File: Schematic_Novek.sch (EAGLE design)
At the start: 46 parts, among them IC1 STM32F10XCXT6, J2 1X2-3.5MM, J3 1X2-3.5MM, Q1 2N2907, U1 BQ21040, U2 MAX17048G+T10, U3 HX711

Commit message: Component placement on board
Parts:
- removed JP3: (no value), pinhead:PINHD-1X4
- removed R1: (no value), resistor:R-EU_0204/7
- added R13: 1M, SparkFun-Resistors:1MOHM-0603-1/4W-5%
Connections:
- removed net 5V: JP3.3
- removed net FTDI_RX: IC1PORTA_H.PA9, JP3.1
- removed net FTDI_TX: IC1PORTA_H.PA10, JP3.2
- net GND: now also J1.SHIELD, J2.1; no longer JP3.4
- net OSCIN: now also R13.2; no longer R1.2
- net OSCOUT: now also R13.1; no longer R1.1
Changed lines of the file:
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@@
 <part name="C1" library="SparkFun-Capacitors" deviceset="22PF" device="-0603-50V-5%" value="22pF"/>
 <part name="C2" library="SparkFun-Capacitors" deviceset="22PF" device="-0603-50V-5%" value="22pF"/>
-<part name="R1" library="resistor" deviceset="R-EU_" device="0204/7"/>
 <part name="JP1" library="pinhead" library_urn="urn:adsk.eagle:library:325" deviceset="PINHD-1X4" device="/90" package3d_urn="urn:adsk.eagle:package:22404/2" value="SWD"/>
 <part name="FRAME2" library="frames" deviceset="A4L-LOC" device=""/>
@@
 <part name="R3" library="SparkFun-Resistors" deviceset="100KOHM" device="-0603-1/10W-1%" value="100k"/>
 <part name="R4" library="SparkFun-Resistors" deviceset="100KOHM" device="-0603-1/10W-1%" value="100k"/>
-<part name="JP3" library="pinhead" library_urn="urn:adsk.eagle:library:325" deviceset="PINHD-1X4" device="" package3d_urn="urn:adsk.eagle:package:22407/2"/>
 <part name="J1" library="SparkFun-Connectors" deviceset="USB_MICRO-B" device="_FEMALE-SMT"/>
 <part name="SUPPLY15" library="supply2" deviceset="GND" device=""/>
@@
 <part name="J4" library="SparkFun-Connectors" deviceset="CONN_03" device="JST-PTH"/>
 <part name="R12" library="SparkFun-Resistors" deviceset="10KOHM" device="-0603-1/10W-1%" value="10k"/>
+<part name="R13" library="SparkFun-Resistors" deviceset="1MOHM" device="-0603-1/4W-5%" value="1M"/>
 </parts>
 <sheets>
@@
 <attribute name="VALUE" x="185.841" y="74.476" size="1.778" layer="96" font="vector" rot="R270"/>
 </instance>
-<instance part="R1" gate="G$1" x="173" y="81" smashed="yes" rot="R90">
-<attribute name="NAME" x="171.5014" y="77.19" size="1.778" layer="95" rot="R90"/>
-<attribute name="VALUE" x="176.302" y="77.19" size="1.778" layer="96" rot="R90"/>
-</instance>
 <instance part="JP1" gate="A" x="30.96" y="98.46" smashed="yes" rot="MR0">
 <attribute name="NAME" x="37.31" y="106.715" size="1.778" layer="95" rot="MR0"/>
@@
 <attribute name="VALUE" x="194" y="101.476" size="1.778" layer="96" font="vector" align="top-center"/>
 </instance>
-<instance part="JP3" gate="A" x="32" y="47" smashed="yes" rot="MR0">
-<attribute name="NAME" x="38.35" y="55.255" size="1.778" layer="95" rot="MR0"/>
-<attribute name="VALUE" x="38.35" y="39.38" size="1.778" layer="96" rot="MR0"/>
+<instance part="R13" gate="G$1" x="173" y="81" smashed="yes" rot="R90">
+<attribute name="NAME" x="171.476" y="81" size="1.778" layer="95" font="vector" rot="R90" align="bottom-center"/>
+<attribute name="VALUE" x="174.524" y="81" size="1.778" layer="96" font="vector" rot="R90" align="top-center"/>
 </instance>
 </instances>
@@
 <wire x1="180" y1="83.54" x2="180" y2="87" width="0.1524" layer="91"/>
 <wire x1="180" y1="87" x2="185.46" y2="87" width="0.1524" layer="91"/>
-<pinref part="R1" gate="G$1" pin="2"/>
-<wire x1="173" y1="87" x2="180" y2="87" width="0.1524" layer="91"/>
 <junction x="180" y="87"/>
-<wire x1="173" y1="86.08" x2="173" y2="87" width="0.1524" layer="91"/>
 <wire x1="173" y1="87" x2="160" y2="87" width="0.1524" layer="91"/>
 <label x="160" y="87" size="1.778" layer="95"/>
+<pinref part="R13" gate="G$1" pin="2"/>
+<wire x1="173" y1="86.08" x2="173" y2="87" width="0.1524" layer="91"/>
+<wire x1="173" y1="87" x2="180" y2="87" width="0.1524" layer="91"/>
 </segment>
 </net>
@@
 <wire x1="180" y1="78.46" x2="180" y2="76" width="0.1524" layer="91"/>
 <wire x1="180" y1="76" x2="185.46" y2="76" width="0.1524" layer="91"/>
-<pinref part="R1" gate="G$1" pin="1"/>
-<wire x1="173" y1="76" x2="180" y2="76" width="0.1524" layer="91"/>
 <junction x="180" y="76"/>
-<wire x1="173" y1="75.92" x2="173" y2="76" width="0.1524" layer="91"/>
 <wire x1="173" y1="76" x2="160" y2="76" width="0.1524" layer="91"/>
 <label x="160" y="76" size="1.778" layer="95"/>
+<pinref part="R13" gate="G$1" pin="1"/>
+<wire x1="173" y1="75.92" x2="173" y2="76" width="0.1524" layer="91"/>
+<wire x1="173" y1="76" x2="180" y2="76" width="0.1524" layer="91"/>
 </segment>
 </net>
@@
 <pinref part="JP2" gate="A" pin="6"/>
 <wire x1="190" y1="100.52" x2="183.26" y2="100.52" width="0.1524" layer="91"/>
-</segment>
-<segment>
-<pinref part="JP3" gate="A" pin="4"/>
-<wire x1="34.54" y1="44.46" x2="45" y2="44.46" width="0.1524" layer="91"/>
-<label x="45" y="45" size="1.778" layer="95"/>
 </segment>
 </net>
@@
 </segment>
 </net>
-<net name="FTDI_RX" class="0">
-<segment>
-<pinref part="JP3" gate="A" pin="1"/>
-<wire x1="34.54" y1="52.08" x2="45" y2="52.08" width="0.1524" layer="91"/>
-<label x="45" y="52" size="1.778" layer="95"/>
-</segment>
-<segment>
-<pinref part="IC1" gate="PORTA_H" pin="PA9"/>
-<wire x1="101.6" y1="104.14" x2="91" y2="104.14" width="0.1524" layer="91"/>
-<label x="91" y="105" size="1.778" layer="95"/>
-</segment>
-</net>
-<net name="FTDI_TX" class="0">
-<segment>
-<pinref part="JP3" gate="A" pin="2"/>
-<wire x1="34.54" y1="49.54" x2="45" y2="49.54" width="0.1524" layer="91"/>
-<label x="45" y="50" size="1.778" layer="95"/>
-</segment>
-<segment>
-<pinref part="IC1" gate="PORTA_H" pin="PA10"/>
-<wire x1="101.6" y1="101.6" x2="91" y2="101.6" width="0.1524" layer="91"/>
-<label x="91" y="102" size="1.778" layer="95"/>
-</segment>
-</net>
-<net name="5V" class="0">
-<segment>
-<pinref part="JP3" gate="A" pin="3"/>
-<wire x1="34.54" y1="47" x2="45" y2="47" width="0.1524" layer="91"/>
-<label x="45" y="47" size="1.778" layer="95"/>
-</segment>
-</net>
 <net name="SDA" class="0">
 <segment>
@@
 <pinref part="SUPPLY15" gate="GND" pin="GND"/>
 <junction x="49" y="130.54"/>
+<pinref part="J1" gate="G$1" pin="SHIELD"/>
+<wire x1="41.08" y1="130.92" x2="49" y2="130.92" width="0.1524" layer="91"/>
+<wire x1="49" y1="130.92" x2="49" y2="130.54" width="0.1524" layer="91"/>
 </segment>
 <segment>
@@
 <label x="53" y="48" size="1.778" layer="95"/>
 </segment>
-</net>
+<segment>
+<pinref part="J2" gate="G$1" pin="1"/>
+<pinref part="SUPPLY33" gate="GND" pin="GND"/>
+<wire x1="16.08" y1="141.46" x2="16.08" y2="141" width="0.1524" layer="91"/>
+<wire x1="16.08" y1="141" x2="20.46" y2="141" width="0.1524" layer="91"/>
+</segment>
+</net>

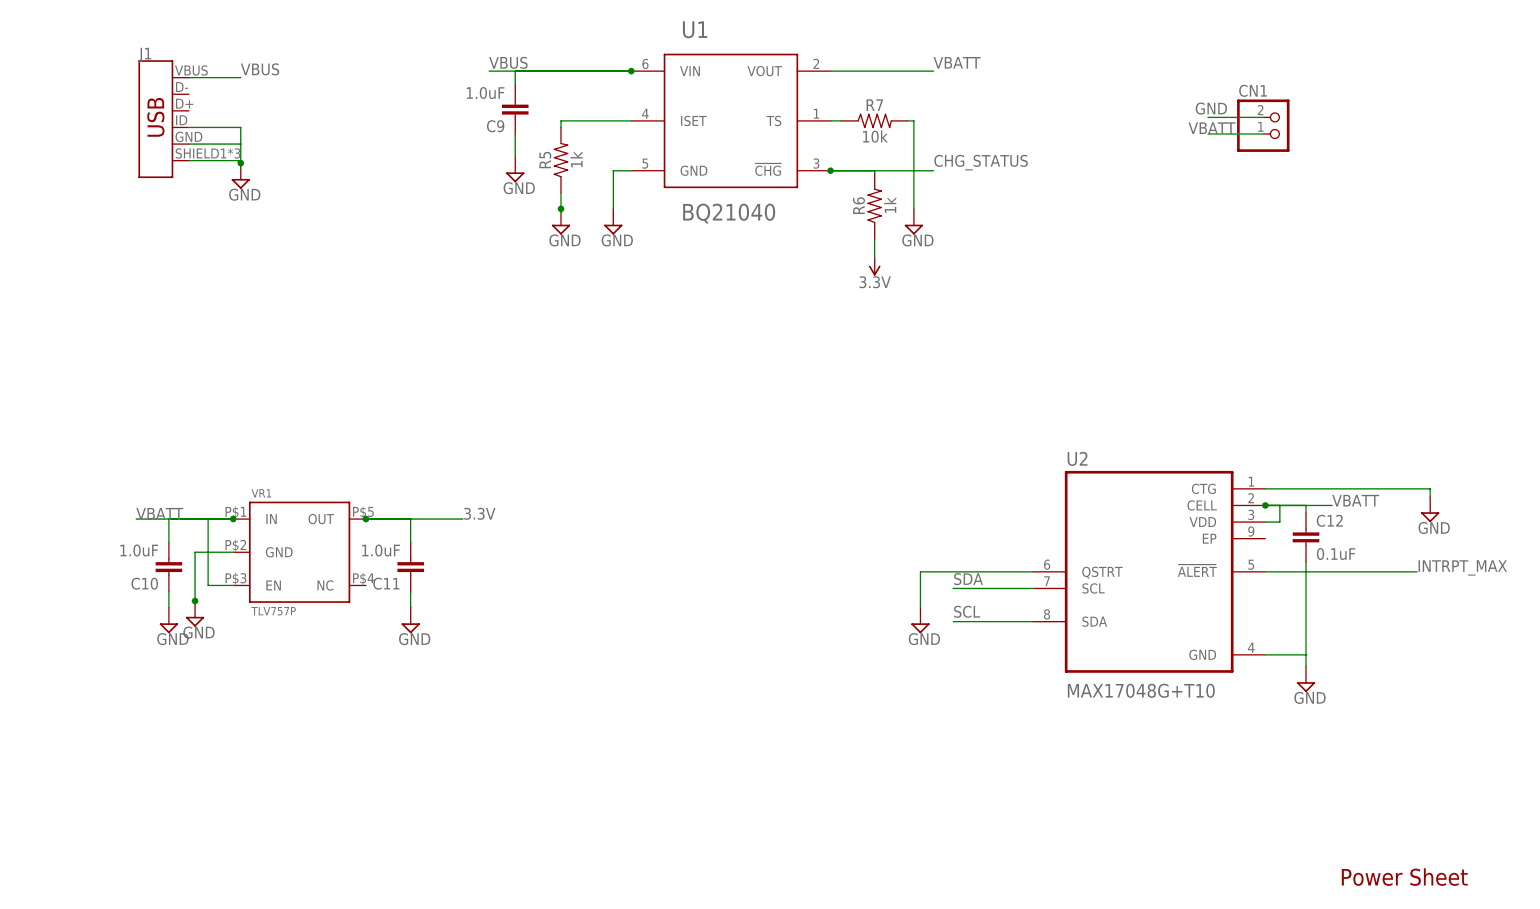
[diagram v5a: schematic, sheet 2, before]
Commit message: Completes routing
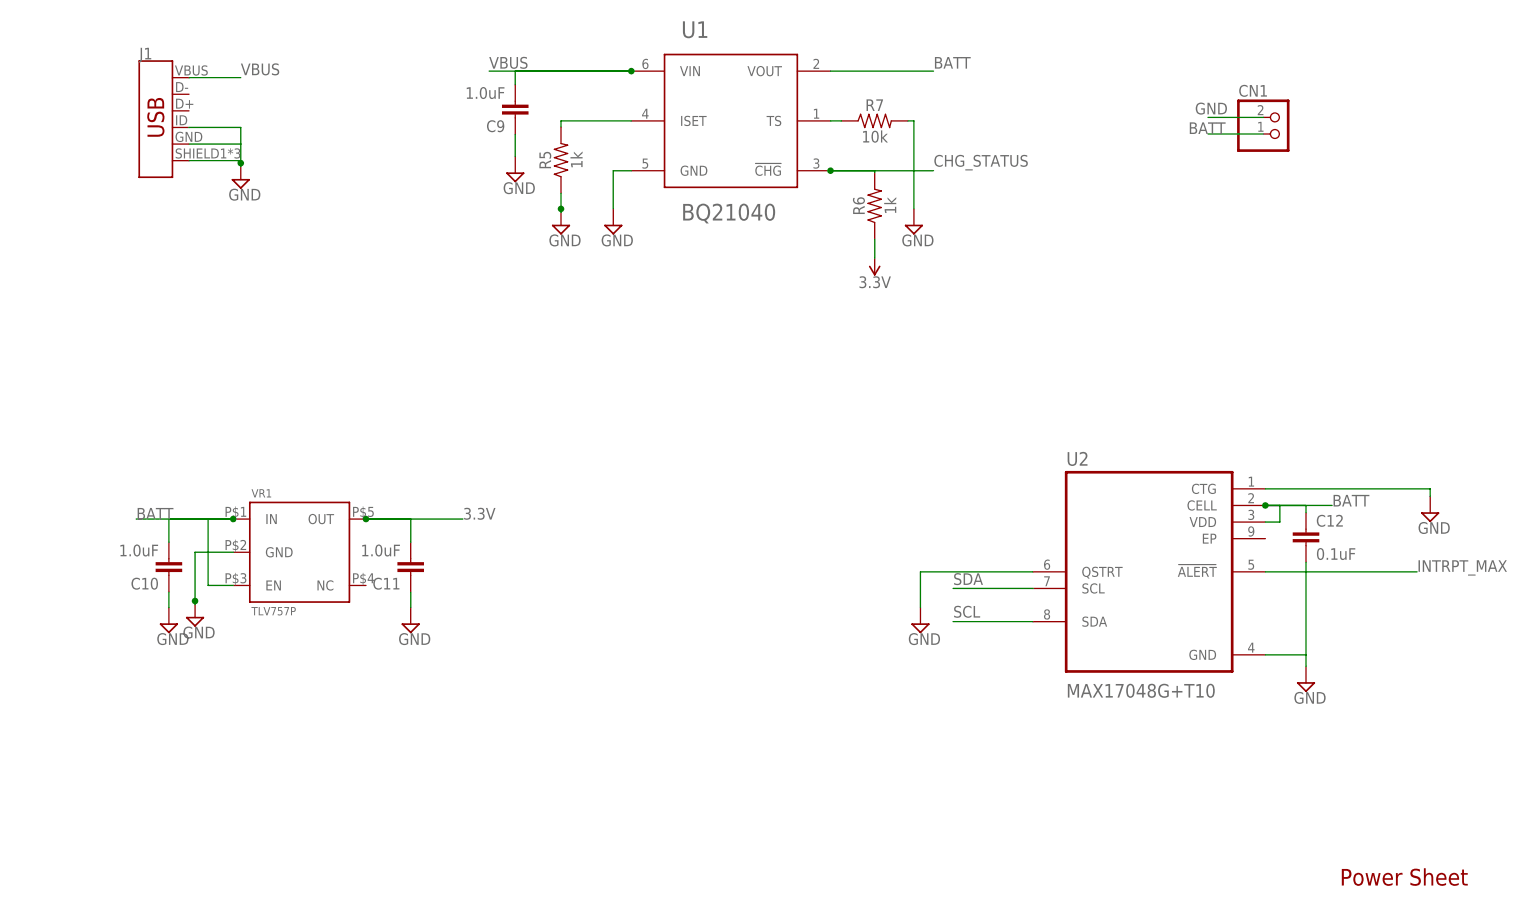
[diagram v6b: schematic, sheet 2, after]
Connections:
- net VBATT renamed BATT
- new net VBHT: IC1AN_POWER.VBAT
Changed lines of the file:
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@@
 <setting verticaltext="up"/>
 </settings>
-<grid distance="1" unitdist="mm" unit="mm" style="dots" multiple="1" display="yes" altdistance="1" altunitdist="mm" altunit="mm"/>
+<grid distance="0.1" unitdist="inch" unit="inch" style="lines" multiple="1" display="no" altdistance="0.01" altunitdist="inch" altunit="inch"/>
 <layers>
-<layer number="1" name="Top" color="4" fill="1" visible="yes" active="no"/>
-<layer number="2" name="Route2" color="16" fill="1" visible="yes" active="no"/>
-<layer number="3" name="Route3" color="17" fill="1" visible="yes" active="no"/>
-<layer number="4" name="Route4" color="18" fill="1" visible="yes" active="no"/>
-<layer number="5" name="Route5" color="19" fill="1" visible="yes" active="no"/>
-<layer number="6" name="Route6" color="25" fill="1" visible="yes" active="no"/>
-<layer number="7" name="Route7" color="26" fill="1" visible="yes" active="no"/>
-<layer number="8" name="Route8" color="27" fill="1" visible="yes" active="no"/>
-<layer number="9" name="Route9" color="28" fill="1" visible="yes" active="no"/>
-<layer number="10" name="Route10" color="29" fill="1" visible="yes" active="no"/>
-<layer number="11" name="Route11" color="30" fill="1" visible="yes" active="no"/>
-<layer number="12" name="Route12" color="20" fill="1" visible="yes" active="no"/>
-<layer number="13" name="Route13" color="21" fill="1" visible="yes" active="no"/>
-<layer number="14" name="Route14" color="22" fill="1" visible="yes" active="no"/>
-<layer number="15" name="Route15" color="23" fill="1" visible="yes" active="no"/>
-<layer number="16" name="Bottom" color="1" fill="1" visible="yes" active="no"/>
-<layer number="17" name="Pads" color="2" fill="1" visible="yes" active="no"/>
-<layer number="18" name="Vias" color="2" fill="1" visible="yes" active="no"/>
-<layer number="19" name="Unrouted" color="6" fill="1" visible="yes" active="no"/>
-<layer number="20" name="Dimension" color="24" fill="1" visible="yes" active="no"/>
-<layer number="21" name="tPlace" color="7" fill="1" visible="yes" active="no"/>
-<layer number="22" name="bPlace" color="7" fill="1" visible="yes" active="no"/>
-<layer number="23" name="tOrigins" color="15" fill="1" visible="yes" active="no"/>
-<layer number="24" name="bOrigins" color="15" fill="1" visible="yes" active="no"/>
-<layer number="25" name="tNames" color="7" fill="1" visible="yes" active="no"/>
-<layer number="26" name="bNames" color="7" fill="1" visible="yes" active="no"/>
-<layer number="27" name="tValues" color="7" fill="1" visible="yes" active="no"/>
-<layer number="28" name="bValues" color="7" fill="1" visible="yes" active="no"/>
+<layer number="1" name="Top" color="4" fill="1" visible="no" active="no"/>
+<layer number="2" name="Route2" color="16" fill="1" visible="no" active="no"/>
+<layer number="3" name="Route3" color="17" fill="1" visible="no" active="no"/>
+<layer number="4" name="Route4" color="18" fill="1" visible="no" active="no"/>
+<layer number="5" name="Route5" color="19" fill="1" visible="no" active="no"/>
+<layer number="6" name="Route6" color="25" fill="1" visible="no" active="no"/>
+<layer number="7" name="Route7" color="26" fill="1" visible="no" active="no"/>
+<layer number="8" name="Route8" color="27" fill="1" visible="no" active="no"/>
+<layer number="9" name="Route9" color="28" fill="1" visible="no" active="no"/>
+<layer number="10" name="Route10" color="29" fill="1" visible="no" active="no"/>
+<layer number="11" name="Route11" color="30" fill="1" visible="no" active="no"/>
+<layer number="12" name="Route12" color="20" fill="1" visible="no" active="no"/>
+<layer number="13" name="Route13" color="21" fill="1" visible="no" active="no"/>
+<layer number="14" name="Route14" color="22" fill="1" visible="no" active="no"/>
+<layer number="15" name="Route15" color="23" fill="1" visible="no" active="no"/>
+<layer number="16" name="Bottom" color="1" fill="1" visible="no" active="no"/>
+<layer number="17" name="Pads" color="2" fill="1" visible="no" active="no"/>
+<layer number="18" name="Vias" color="2" fill="1" visible="no" active="no"/>
+<layer number="19" name="Unrouted" color="6" fill="1" visible="no" active="no"/>
+<layer number="20" name="Dimension" color="24" fill="1" visible="no" active="no"/>
+<layer number="21" name="tPlace" color="7" fill="1" visible="no" active="no"/>
+<layer number="22" name="bPlace" color="7" fill="1" visible="no" active="no"/>
+<layer number="23" name="tOrigins" color="15" fill="1" visible="no" active="no"/>
+<layer number="24" name="bOrigins" color="15" fill="1" visible="no" active="no"/>
+<layer number="25" name="tNames" color="7" fill="1" visible="no" active="no"/>
+<layer number="26" name="bNames" color="7" fill="1" visible="no" active="no"/>
+<layer number="27" name="tValues" color="7" fill="1" visible="no" active="no"/>
+<layer number="28" name="bValues" color="7" fill="1" visible="no" active="no"/>
 <layer number="29" name="tStop" color="7" fill="3" visible="no" active="no"/>
 <layer number="30" name="bStop" color="7" fill="6" visible="no" active="no"/>
@@
 <layer number="35" name="tGlue" color="7" fill="4" visible="no" active="no"/>
 <layer number="36" name="bGlue" color="7" fill="5" visible="no" active="no"/>
-<layer number="37" name="tTest" color="7" fill="1" visible="yes" active="no"/>
-<layer number="38" name="bTest" color="7" fill="1" visible="yes" active="no"/>
+<layer number="37" name="tTest" color="7" fill="1" visible="no" active="no"/>
+<layer number="38" name="bTest" color="7" fill="1" visible="no" active="no"/>
 <layer number="39" name="tKeepout" color="4" fill="11" visible="no" active="no"/>
 <layer number="40" name="bKeepout" color="1" fill="11" visible="no" active="no"/>
@@
 <layer number="44" name="Drills" color="7" fill="1" visible="no" active="no"/>
 <layer number="45" name="Holes" color="7" fill="1" visible="no" active="no"/>
-<layer number="46" name="Milling" color="3" fill="1" visible="yes" active="no"/>
-<layer number="47" name="Measures" color="7" fill="1" visible="yes" active="no"/>
-<layer number="48" name="Document" color="7" fill="1" visible="yes" active="no"/>
-<layer number="49" name="Reference" color="7" fill="1" visible="yes" active="no"/>
-<layer number="50" name="dxf" color="7" fill="1" visible="yes" active="no"/>
-<layer number="51" name="tDocu" color="7" fill="1" visible="yes" active="no"/>
-<layer number="52" name="bDocu" color="7" fill="1" visible="yes" active="no"/>
-<layer number="53" name="tGND_GNDA" color="7" fill="9" visible="yes" active="no"/>
-<layer number="54" name="bGND_GNDA" color="1" fill="9" visible="yes" active="no"/>
-<layer number="56" name="wert" color="7" fill="1" visible="yes" active="no"/>
-<layer number="57" name="tCAD" color="7" fill="1" visible="yes" active="no"/>
-<layer number="59" name="tCarbon" color="7" fill="1" visible="yes" active="no"/>
-<layer number="60" name="bCarbon" color="7" fill="1" visible="yes" active="no"/>
+<layer number="46" name="Milling" color="3" fill="1" visible="no" active="no"/>
+<layer number="47" name="Measures" color="7" fill="1" visible="no" active="no"/>
+<layer number="48" name="Document" color="7" fill="1" visible="no" active="no"/>
+<layer number="49" name="Reference" color="7" fill="1" visible="no" active="no"/>
+<layer number="50" name="dxf" color="7" fill="1" visible="no" active="no"/>
+<layer number="51" name="tDocu" color="7" fill="1" visible="no" active="no"/>
+<layer number="52" name="bDocu" color="7" fill="1" visible="no" active="no"/>
+<layer number="53" name="tGND_GNDA" color="7" fill="9" visible="no" active="no"/>
+<layer number="54" name="bGND_GNDA" color="1" fill="9" visible="no" active="no"/>
+<layer number="56" name="wert" color="7" fill="1" visible="no" active="no"/>
+<layer number="57" name="tCAD" color="7" fill="1" visible="no" active="no"/>
+<layer number="59" name="tCarbon" color="7" fill="1" visible="no" active="no"/>
+<layer number="60" name="bCarbon" color="7" fill="1" visible="no" active="no"/>
 <layer number="88" name="SimResults" color="9" fill="1" visible="yes" active="yes"/>
 <layer number="89" name="SimProbes" color="9" fill="1" visible="yes" active="yes"/>
@@
 </segment>
 </net>
+<net name="VBHT" class="0">
+<segment>
+<pinref part="IC1" gate="AN_POWER" pin="VBAT"/>
+<wire x1="137.16" y1="71.12" x2="147.32" y2="71.12" width="0.1524" layer="91"/>
+<label x="147.32" y="71.12" size="1.778" layer="95"/>
+</segment>
+</net>
 </nets>
 </sheet>
@@
 </segment>
 </net>
-<net name="VBATT" class="0">
+<net name="SDA" class="0">
+<segment>
+<pinref part="U2" gate="G$1" pin="SCL"/>
+<wire x1="170.22" y1="65.46" x2="158" y2="65.46" width="0.1524" layer="91"/>
+<label x="158" y="66" size="1.778" layer="95"/>
+</segment>
+</net>
+<net name="SCL" class="0">
+<segment>
+<pinref part="U2" gate="G$1" pin="SDA"/>
+<wire x1="170.22" y1="60.38" x2="158" y2="60.38" width="0.1524" layer="91"/>
+<label x="158" y="61" size="1.778" layer="95"/>
+</segment>
+</net>
+<net name="INTRPT_MAX" class="0">
+<segment>
+<pinref part="U2" gate="G$1" pin="!ALERT"/>
+<wire x1="205.78" y1="68" x2="229" y2="68" width="0.1524" layer="91"/>
+<label x="229" y="68" size="1.778" layer="95"/>
+</segment>
+</net>
+<net name="BATT" class="0">
 <segment>
 <pinref part="U1" gate="G$1" pin="VOUT"/>
@@
 </segment>
 </net>
-<net name="SDA" class="0">
-<segment>
-<pinref part="U2" gate="G$1" pin="SCL"/>
-<wire x1="170.22" y1="65.46" x2="158" y2="65.46" width="0.1524" layer="91"/>
-<label x="158" y="66" size="1.778" layer="95"/>
-</segment>
-</net>
-<net name="SCL" class="0">
-<segment>
-<pinref part="U2" gate="G$1" pin="SDA"/>
-<wire x1="170.22" y1="60.38" x2="158" y2="60.38" width="0.1524" layer="91"/>
-<label x="158" y="61" size="1.778" layer="95"/>
-</segment>
-</net>
-<net name="INTRPT_MAX" class="0">
-<segment>
-<pinref part="U2" gate="G$1" pin="!ALERT"/>
-<wire x1="205.78" y1="68" x2="229" y2="68" width="0.1524" layer="91"/>
-<label x="229" y="68" size="1.778" layer="95"/>
-</segment>
-</net>
